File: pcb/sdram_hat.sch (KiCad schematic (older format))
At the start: 34 parts, among them J1 CONN_02X20, J2 CONN_02X20, J3 CONN_02X20, J4 CONN_02X20, J5 AUDIO_OUT_JACK

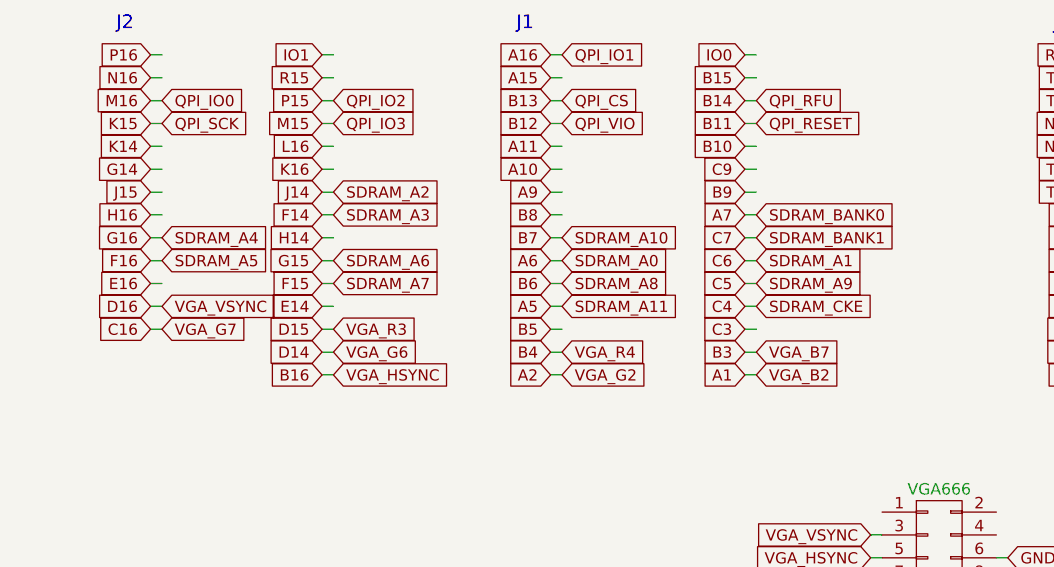
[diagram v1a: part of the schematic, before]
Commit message: Length match QPI flash and SDRAM traces
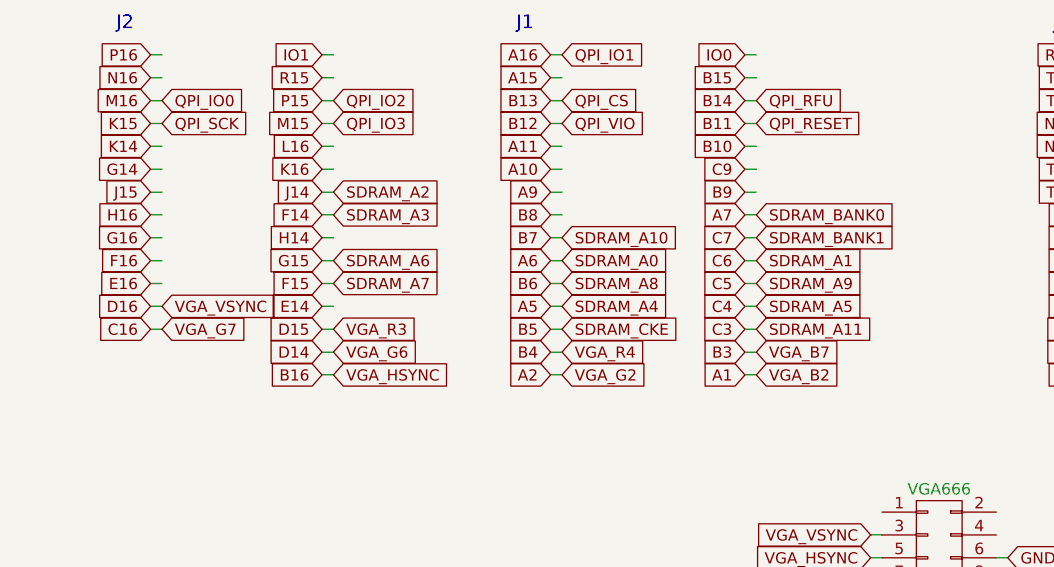
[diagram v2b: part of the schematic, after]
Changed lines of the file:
@@
 Text GLabel 7350 4400 2    49   Input ~ 0
 SDRAM_A3
-Text GLabel 6600 4500 2    49   Input ~ 0
+Text GLabel 8350 4800 2    49   Input ~ 0
 SDRAM_A4
-Text GLabel 6600 4600 2    49   Input ~ 0
+Text GLabel 9200 4800 2    49   Input ~ 0
 SDRAM_A5
 Text GLabel 7350 4600 2    49   Input ~ 0
@@
 Text GLabel 8350 4500 2    49   Input ~ 0
 SDRAM_A10
-Text GLabel 8350 4800 2    49   Input ~ 0
+Text GLabel 9200 4900 2    49   Input ~ 0
 SDRAM_A11
 Text GLabel 9200 4400 2    49   Input ~ 0
@@
 Text GLabel 11650 4800 2    49   Input ~ 0
 SDRAM_CLK
-Text GLabel 9200 4800 2    49   Input ~ 0
+Text GLabel 8350 4900 2    49   Input ~ 0
 SDRAM_CKE
 Text GLabel 11650 4100 2    49   Input ~ 0

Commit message: Very misalign. Wow. Much fix.
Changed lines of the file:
@@
 Text GLabel 11650 4400 2    49   Input ~ 0
 SDRAM_D0
-Text GLabel 9200 4000 2    49   Input ~ 0
+Text GLabel 8350 4000 2    49   Input ~ 0
 QPI_RESET
 Text GLabel 9200 3900 2    49   Input ~ 0
@@
 Text GLabel 6600 4000 2    49   Input ~ 0
 QPI_SCK
-Text GLabel 8350 4000 2    49   Input ~ 0
+Text GLabel 8350 4100 2    49   Input ~ 0
 QPI_VIO
 Text GLabel 8350 3900 2    49   Input ~ 0
 QPI_CS
-Text GLabel 6600 3900 2    49   Input ~ 0
+Text GLabel 9200 4200 2    49   Input ~ 0
 QPI_IO0
 Text GLabel 8350 3700 2    49   Input ~ 0
 QPI_IO1
-Text GLabel 7350 3900 2    49   Input ~ 0
+Text GLabel 9200 4300 2    49   Input ~ 0
 QPI_IO2
-Text GLabel 7350 4000 2    49   Input ~ 0
+Text GLabel 9200 4000 2    49   Input ~ 0
 QPI_IO3
 Text GLabel 11650 3900 2    49   Input ~ 0
